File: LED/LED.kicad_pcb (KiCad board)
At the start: 2 copper layers, 72.4 x 72.4 mm, 17 parts, among them J1 JST_header

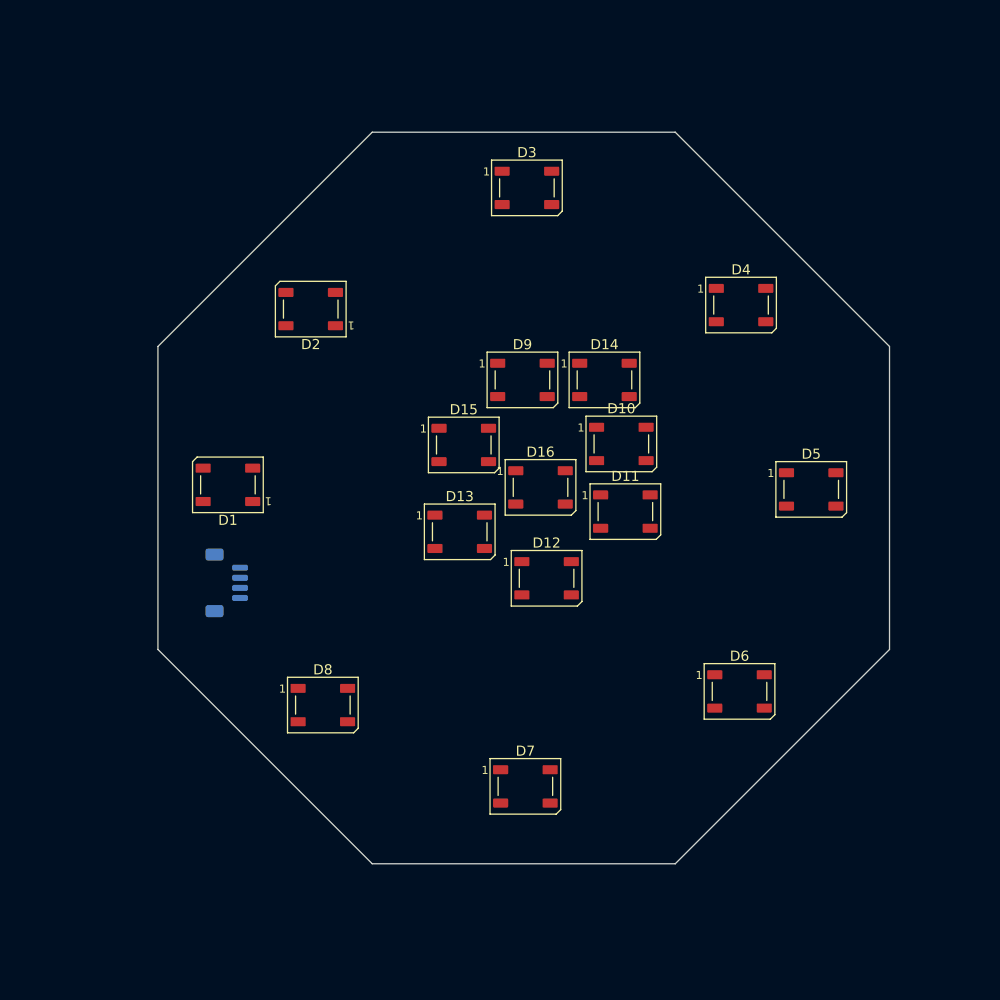
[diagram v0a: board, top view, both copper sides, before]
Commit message: Start work on PCBs, add CC resistors for USB charging
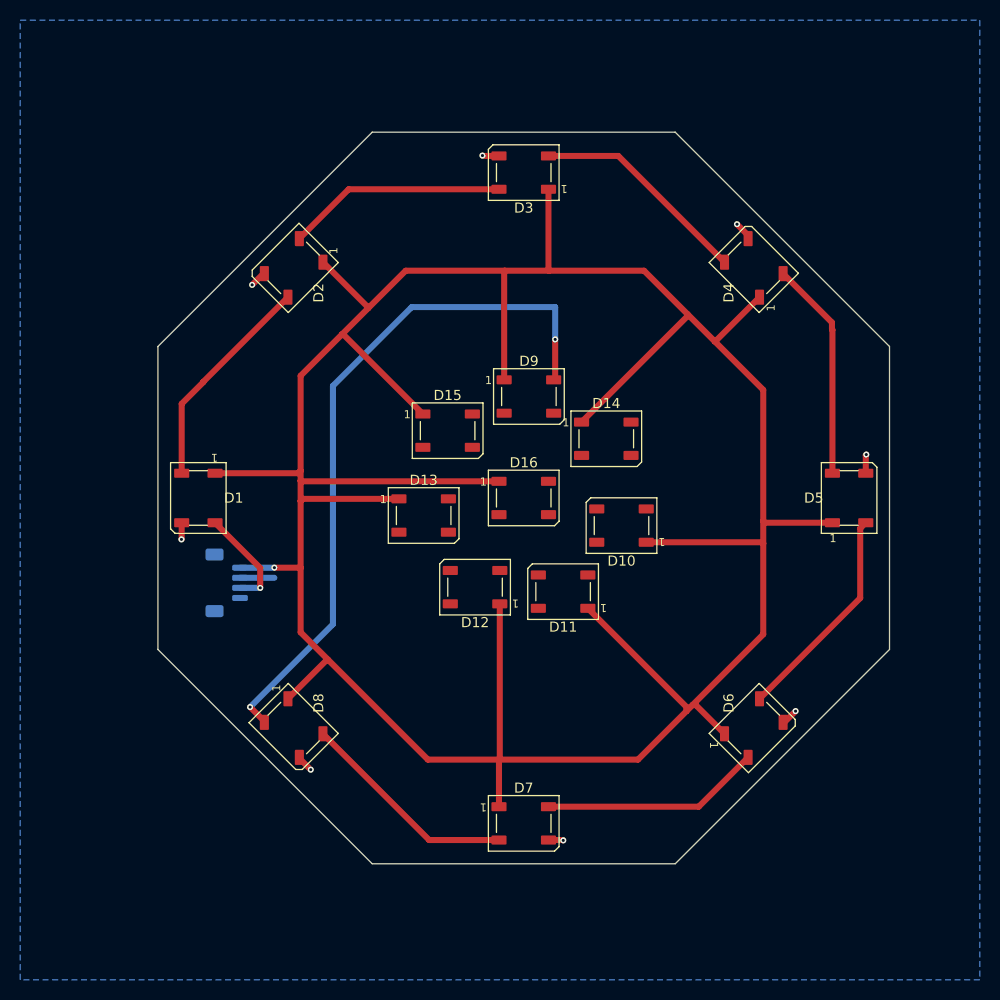
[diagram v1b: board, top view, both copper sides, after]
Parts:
- moved D11 10.0 mm to (160.2, 111.8), turned to 180 degrees
- moved D10 8.08 mm to (166.0, 105.2), turned to 180 degrees
- moved D12 7.14 mm to (151.5, 111.3), turned to 180 degrees
- moved D14 5.83 mm to (164.5, 96.6)
- moved D2 4.41 mm to (133.5, 79.7), turned to -135 degrees
- moved D13 3.92 mm to (146.4, 104.2)
- moved D6 3.89 mm to (179.1, 125.3), turned to 45 degrees
- moved D4 3.89 mm to (179.1, 79.7), turned to 135 degrees
- moved D5 3.84 mm to (188.5, 102.5), turned to 90 degrees
- moved D8 3.68 mm to (133.5, 125.3), turned to -45 degrees
- moved D7 3.67 mm to (156.3, 134.7)
- moved D1 3.20 mm to (124.1, 102.5), turned to -90 degrees
- moved D15 2.13 mm to (148.8, 95.8)
- moved D16 1.97 mm to (156.3, 102.5)
- moved D9 1.76 mm to (156.8, 92.5)
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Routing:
- net /SW_+: track 0.00 -> 325.5 mm, vias 0 -> 1
- net Net-(D8-DOUT): track 0.00 -> 69.8 mm, vias 0 -> 2
- net Net-(D2-DOUT): track 0.00 -> 21.8 mm
- net Net-(D6-DOUT): track 0.00 -> 21.8 mm
- net Net-(D4-DOUT): track 0.00 -> 21.8 mm
- net Net-(D7-DOUT): track 0.00 -> 21.8 mm
- net Net-(D3-DOUT): track 0.00 -> 21.8 mm
- net Net-(D5-DOUT): track 0.00 -> 21.8 mm
- net Net-(D1-DOUT): track 0.00 -> 21.8 mm
- net /BAT_-: track 0.00 -> 17.0 mm, vias 0 -> 8
- net /WS2812B_DIN: track 0.00 -> 10.3 mm, vias 0 -> 1
- added copper zone on B.Cu, net /BAT_-

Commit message: Finish LED PCB
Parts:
- moved D14 19.6 mm to (146.4, 104.2)
- moved D12 8.73 mm to (160.2, 111.8)
- moved D10 8.73 mm to (164.5, 96.6), turned to 0 degrees
- moved D11 8.73 mm to (166.0, 105.2)
- moved D13 8.73 mm to (151.5, 111.3), turned to 180 degrees
- turned D15 to 180 degrees
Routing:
- net Net-(D11-DOUT): track 0.00 -> 16.7 mm
- net Net-(D12-DOUT): track 0.00 -> 14.8 mm
- net Net-(D10-DIN): track 0.00 -> 14.4 mm
- net /SW_+: track 325.5 -> 311.9 mm
- net /BAT_-: track 17.0 -> 28.2 mm, vias 8 -> 16
- net Net-(D10-DOUT): track 0.00 -> 10.6 mm
- net Net-(D15-DOUT): track 0.00 -> 10.3 mm
- net Net-(D14-DOUT): track 0.00 -> 9.38 mm
- net Net-(D13-DOUT): track 0.00 -> 9.20 mm
